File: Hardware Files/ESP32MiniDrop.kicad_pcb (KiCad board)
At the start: 2 copper layers, 74 x 54 mm, 52 parts, among them J1 USB_B_Mini, J2 Barrel_Jack, J3 AudioJack3, J4 Solenoid1 Terminal, J5 0.100" 2x4 Header, Q1 S8050, Q2 S8050, Q3 NMOS 60V 46A, SW1 SPST (RED), SW2 SPST (BLUE)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

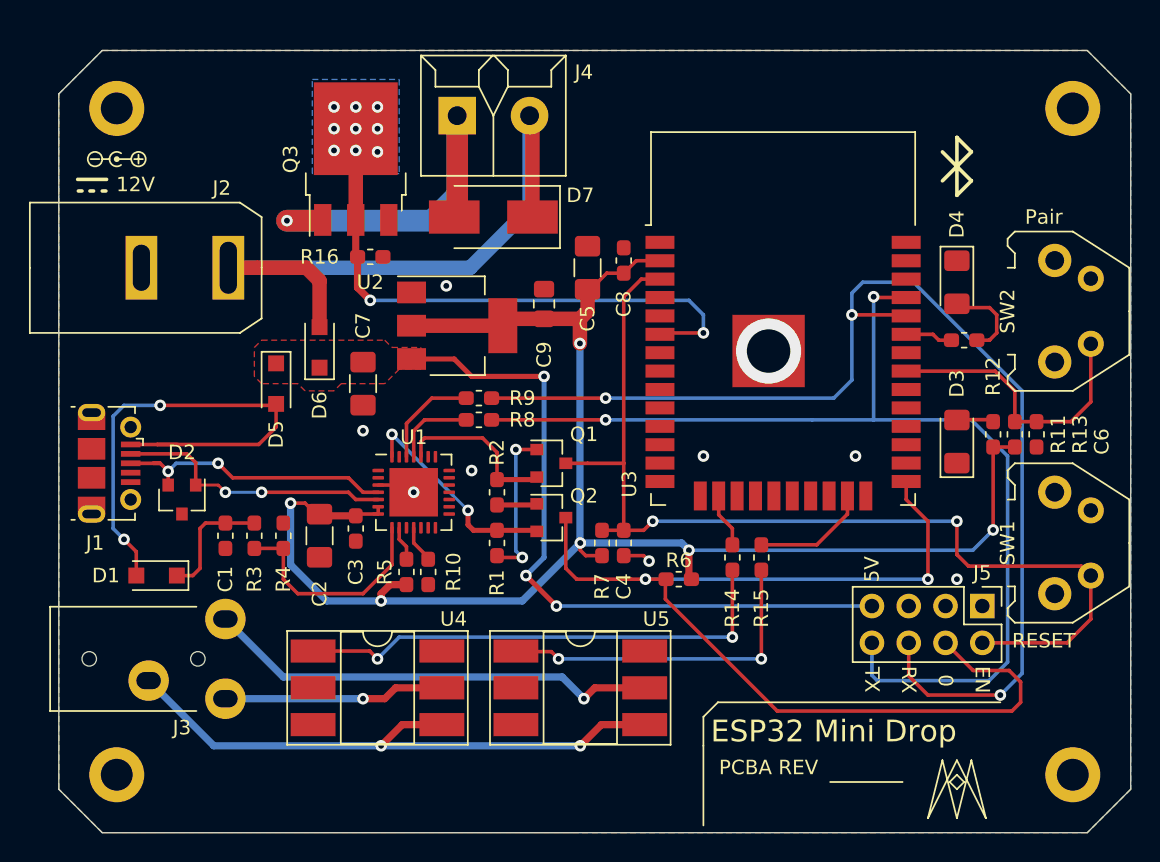
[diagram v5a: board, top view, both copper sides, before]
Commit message: Change mounting holes to M3, update tracks, change solenoid control to pin 8 of ESP32
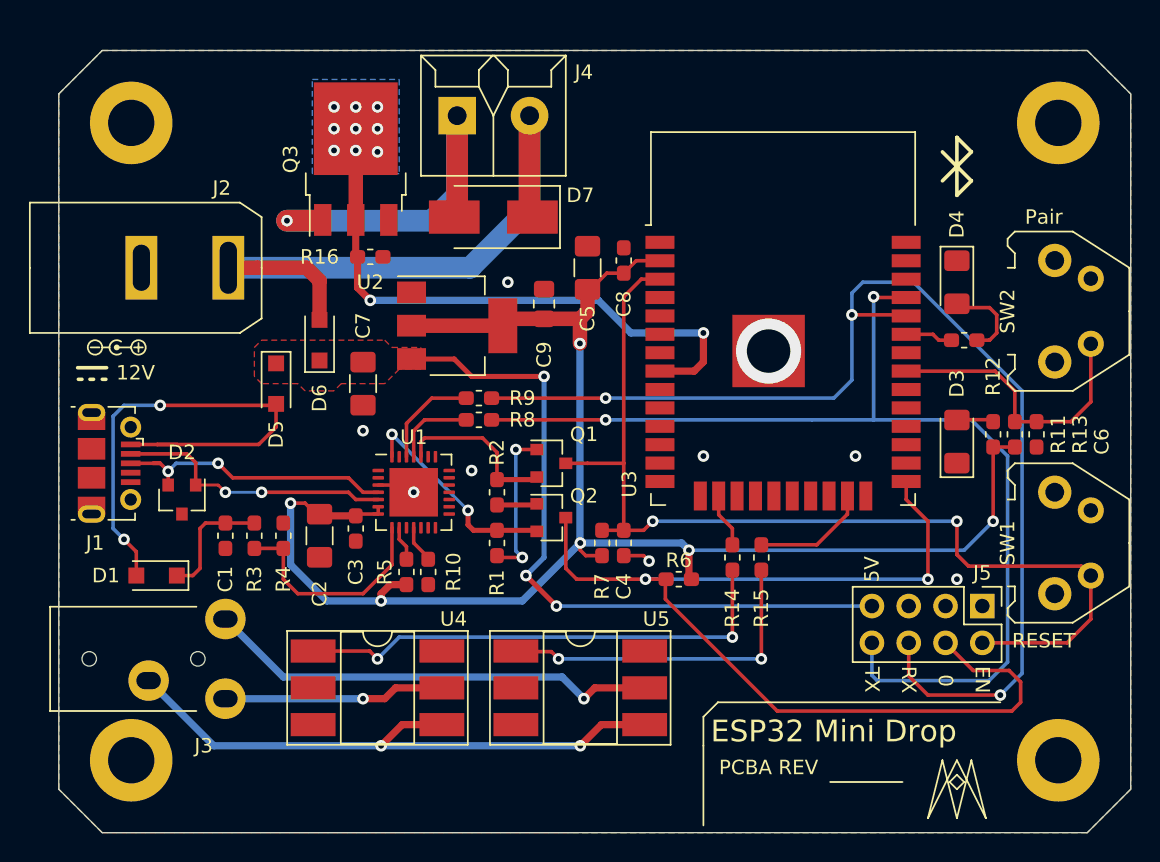
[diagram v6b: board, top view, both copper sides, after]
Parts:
- removed REF** (x4): MountingHole_2.2mm_M2_ISO14580_Pad, MountingHole:MountingHole_2.2mm_M2_ISO14580_Pad
- added M1: Conn_01x01, MountingHole:MountingHole_3.2mm_M3_ISO7380_Pad, F.Cu at (5.00, 5.00)
- added M2: Conn_01x01, MountingHole:MountingHole_3.2mm_M3_ISO7380_Pad, F.Cu at (69.0, 5.00)
- added M3: Conn_01x01, MountingHole:MountingHole_3.2mm_M3_ISO7380_Pad, F.Cu at (5.00, 49.0)
- added M4: Conn_01x01, MountingHole:MountingHole_3.2mm_M3_ISO7380_Pad, F.Cu at (69.0, 49.0)
- moved D6 0.50 mm to (18.0, 20.0)
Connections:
- U3 pad 6: Solenoid_1_CTLO -> Net-(U3-Pad6)
- U3 pad 8: Net-(U3-Pad8) -> Solenoid_1_CTLO
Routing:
- net Solenoid_1_CTLO: track 38.5 -> 40.0 mm

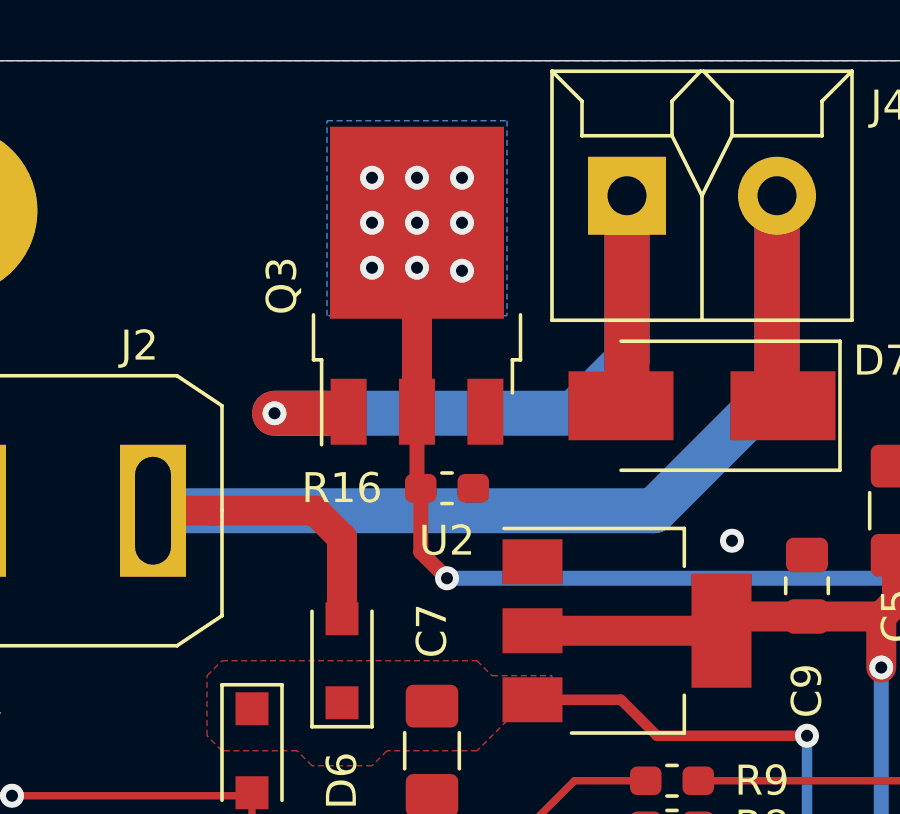
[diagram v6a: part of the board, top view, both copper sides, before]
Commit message: fix Solenoid MOSFET Pin Mapping
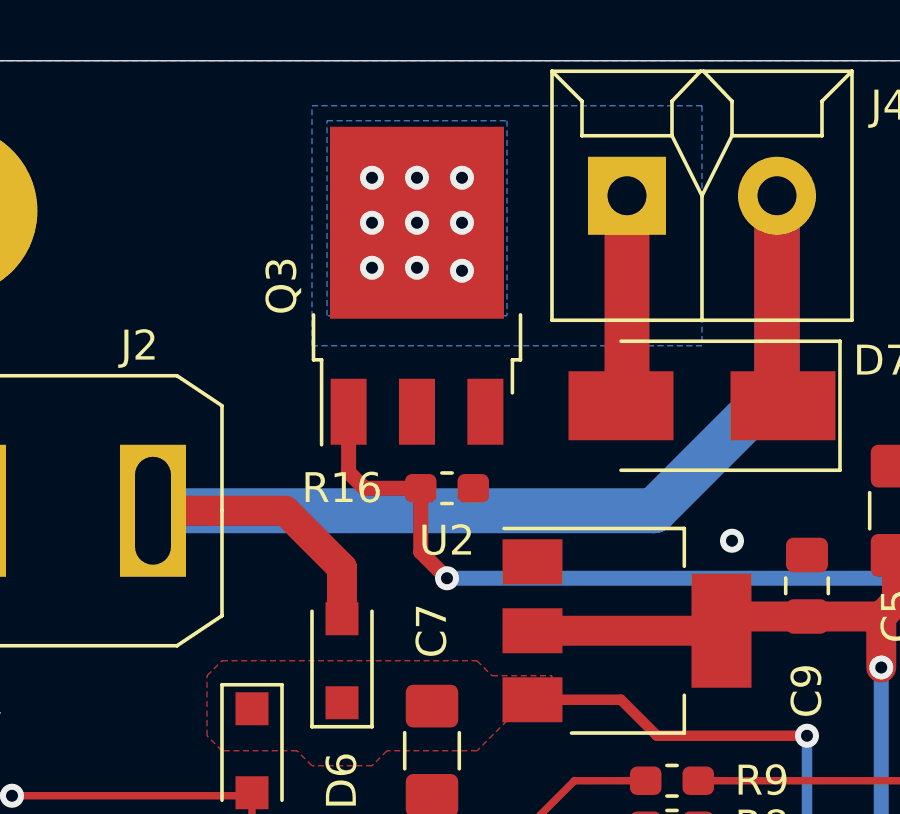
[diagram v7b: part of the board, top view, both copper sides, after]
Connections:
- Q3 pad 1: Net-(D7-Pad2) -> Solenoid_1_CTLO
- Q3 pad 2: Solenoid_1_CTLO -> Net-(D7-Pad2)
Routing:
- net Net-(D7-Pad2): track 28.1 -> 8.38 mm, vias 1 -> 9
- net Solenoid_1_CTLO: track 40.0 -> 37.4 mm, vias 11 -> 2
- net +12V: track 45.6 -> 45.1 mm
- added copper zone on B.Cu, net Net-(D7-Pad2)

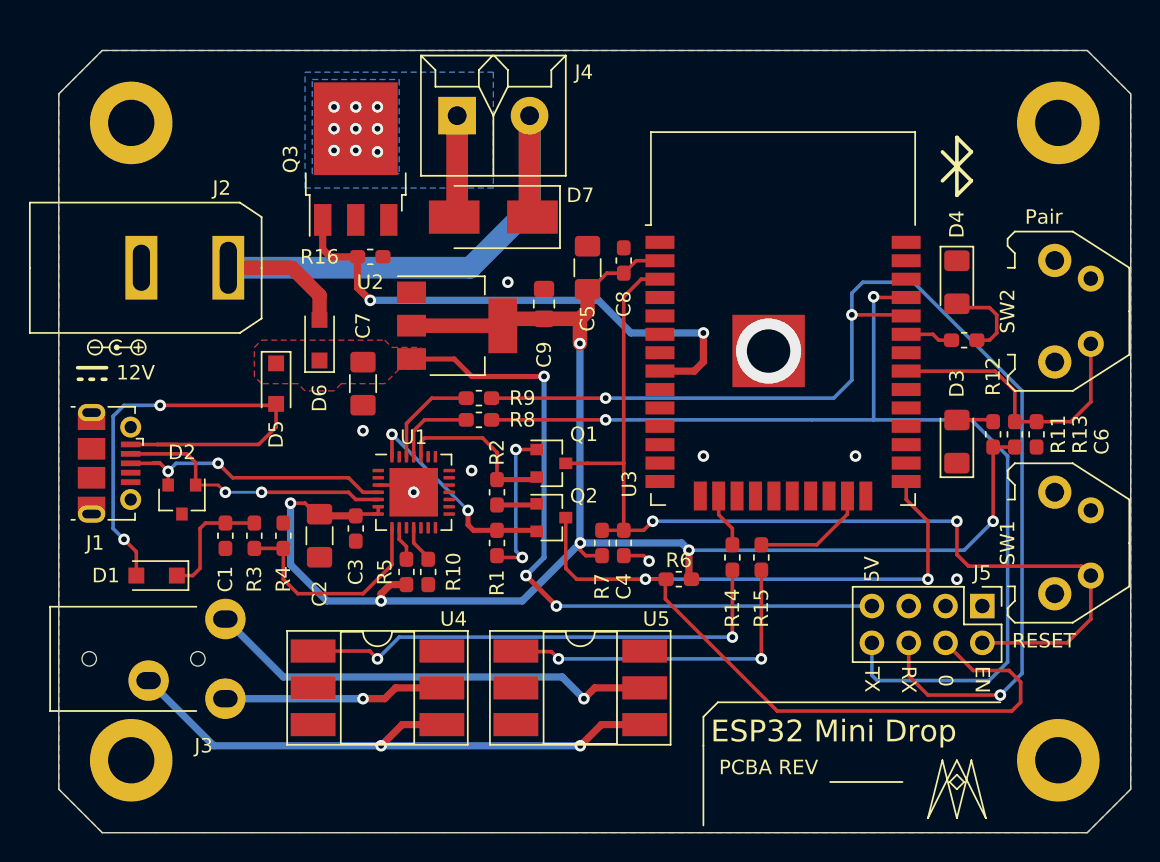
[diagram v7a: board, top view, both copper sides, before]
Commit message: Unroute USB to UART components
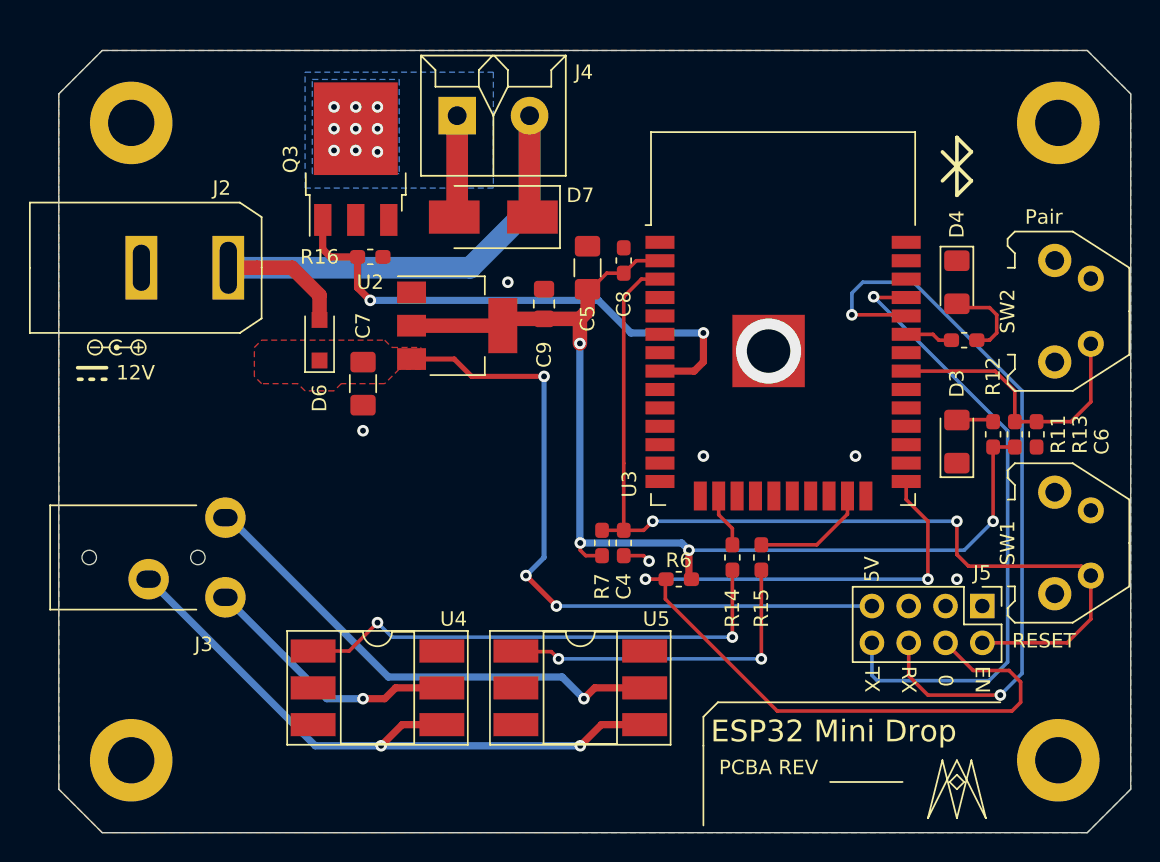
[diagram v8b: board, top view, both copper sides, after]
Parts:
- removed C1, C3: 0.1uF 50V, Capacitor_SMD:C_0603_1608Metric_Pad1.05x0.95mm_HandSolder
- removed C2: 10uF 50V, Capacitor_SMD:C_1206_3216Metric_Pad1.42x1.75mm_HandSolder
- removed D1: 40V 2A, Diode_SMD:D_SOD-123F
- removed D2: SP0502BAHT, Package_TO_SOT_SMD:SOT-23
- removed D5: 20V 1A, Diode_SMD:D_SOD-123F
- removed G***: LOGO, ESP32 Drop Controller:jlcpcblogo
- removed J1: USB_B_Mini, ESP32 Drop Controller:USB_Micro-B_Molex-105017-0001_3D
- removed Q1, Q2: S8050, Package_TO_SOT_SMD:SOT-23
- removed R1, R10, R2: 10k 1% 0.1W, Resistor_SMD:R_0603_1608Metric_Pad1.05x0.95mm_HandSolder
- removed R3: 22.1K 1% 0.1W, Resistor_SMD:R_0603_1608Metric_Pad1.05x0.95mm_HandSolder
- removed R4: 47.5K 1% 0.1W, Resistor_SMD:R_0603_1608Metric_Pad1.05x0.95mm_HandSolder
- removed R5: 2K 1% 0.1W, Resistor_SMD:R_0603_1608Metric_Pad1.05x0.95mm_HandSolder
- removed R8, R9: 0R 0.1W, Resistor_SMD:R_0603_1608Metric_Pad1.05x0.95mm_HandSolder
- removed U1: CP2102N-A01-GQFN28, Package_DFN_QFN:QFN-28-1EP_5x5mm_P0.5mm_EP3.35x3.35mm
- moved J3 7.00 mm to (11.5, 35.0)
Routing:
- net /VUSB: track 36.8 -> 0.00 mm, vias 2 -> 0
- net +3V3: track 112.4 -> 76.0 mm, vias 6 -> 4
- net /USB_RX: track 73.9 -> 43.6 mm, vias 2 -> 1
- net /USB_TX: track 81.3 -> 51.4 mm, vias 3 -> 2
- net /D+: track 19.8 -> 0.00 mm, vias 2 -> 0
- net /D-: track 19.3 -> 0.00 mm, vias 2 -> 0
- net /VBUS: track 15.4 -> 0.00 mm
- net /DTR: track 14.9 -> 0.00 mm, vias 2 -> 0
- net /RTS: track 11.5 -> 0.00 mm
- net Net-(Q1-Pad1): track 10.9 -> 0.00 mm, vias 2 -> 0
- net /IO0: track 74.7 -> 65.4 mm
- net +5V: track 8.46 -> 0.00 mm
- net Net-(R9-Pad2): track 7.15 -> 0.00 mm
- net Net-(R8-Pad2): track 5.74 -> 0.00 mm
- net /EN: track 71.2 -> 67.2 mm
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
